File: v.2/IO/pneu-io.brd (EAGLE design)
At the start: 30.5 x 50.8 mm, 28 parts, among them IC3 ATMEGA328, Q1 16Mhz, U2 NCP1117-5

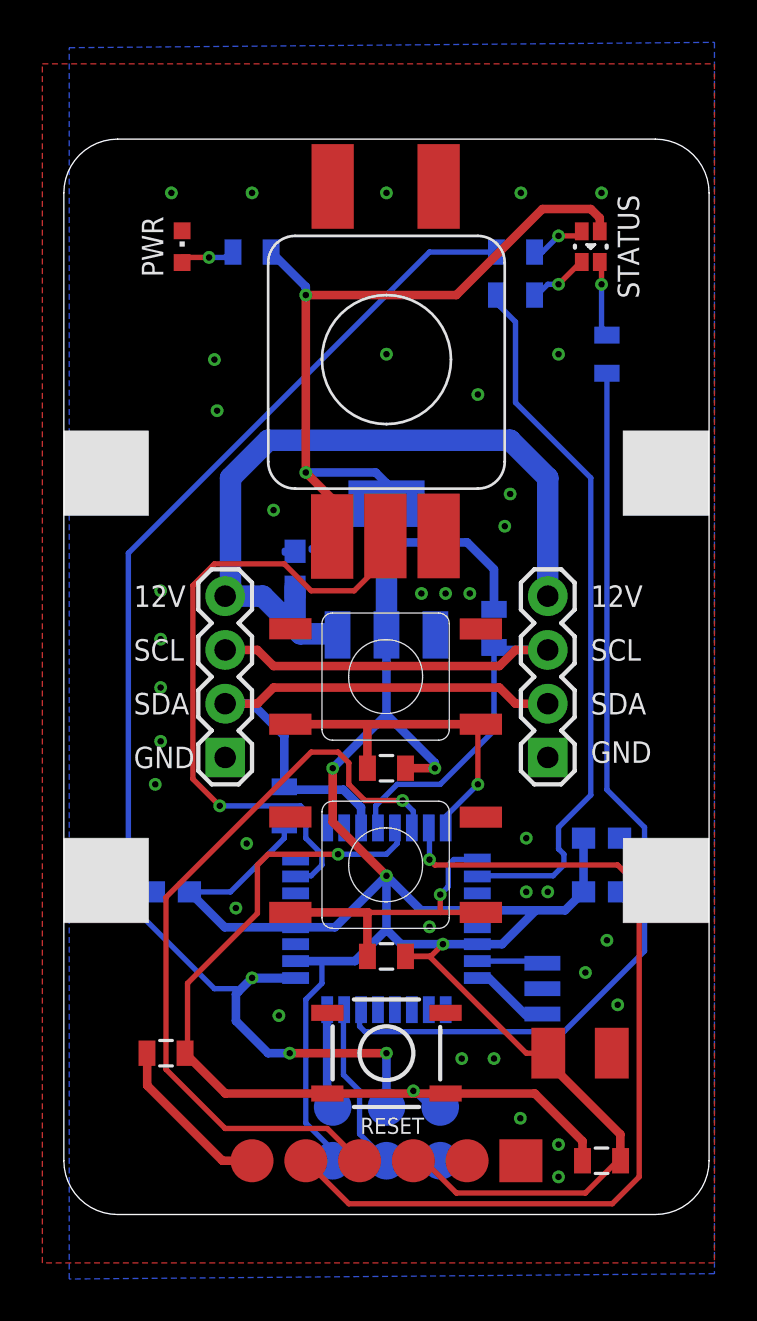
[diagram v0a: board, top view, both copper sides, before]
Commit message: minor changes
getting ready for production:

correct indicator led position on master board
add corner drills to slave boards
generate silk screens
adjust edge connector distance for better fit
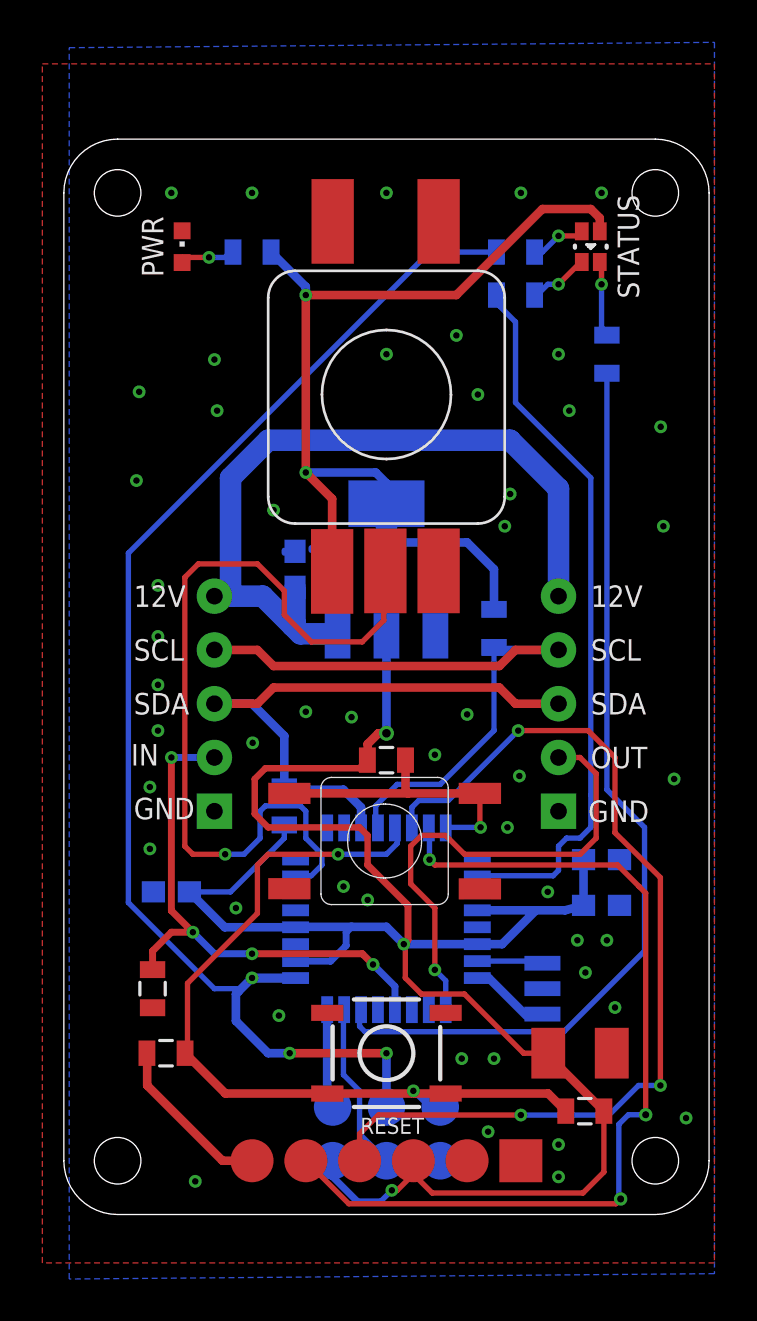
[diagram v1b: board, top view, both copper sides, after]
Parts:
- removed JP2, JP3: (no value), SparkFun-Connectors:1X04
- removed R2: 10K, SparkFun-Resistors:0805
- removed U$3: RS-014R05, digikey:SWITCH-11MM
- added R14: 10k, SparkFun-Resistors:0805
- added U$24, U$27: 1X05, digikey:1X05_TIGHT
- moved U$1 7.75 mm to (12.6, 17.7), turned to 0 degrees
- moved R3 2.47 mm to (22.1, 4.88)
- moved U$2 1.65 mm to (12.7, 39.0)
- moved C10 1.02 mm to (22.9, 16.8)
- moved C8 0.63 mm to (22.9, 14.6)
- moved R1 0.38 mm to (12.7, 21.5), turned to 0 degrees
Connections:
- removed net D5: IC3.9
- new net D5/OUT: IC3.9, U$27.P$4
- net +5V: no longer R2.1
- net D3/BTN: no longer R2.2, U$3.A, U$3.H
- net D8: now also R14.2, U$24.P$4
- net GND: now also R14.1, U$24.P$5, U$27.P$5; no longer JP2.1, JP3.1, U$3.B, U$3.D
- net SCL: now also U$24.P$3, U$27.P$3; no longer JP2.3, JP3.3
- net SDA: now also U$24.P$2, U$27.P$2; no longer JP2.2, JP3.2
- net VIN: now also U$24.P$1, U$27.P$1; no longer JP2.4, JP3.4
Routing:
- net D8: track 0.00 -> 25.6 mm, vias 0 -> 4
- net D5/OUT: track 0.00 -> 23.2 mm, vias 0 -> 1
- net D3/BTN: track 15.0 -> 0.00 mm, vias 1 -> 0
- net A0/POT: track 31.3 -> 42.2 mm
- net RX: track 36.2 -> 45.4 mm, vias 1 -> 3
- net +5V: track 152.0 -> 145.3 mm, vias 6 -> 5
- net D2/BTN: track 16.7 -> 13.9 mm
- net RESET: track 41.3 -> 39.0 mm
- net SDA: track 26.7 -> 28.2 mm
- net SCL: track 30.6 -> 32.1 mm
- net TX: track 42.8 -> 43.7 mm, vias 1 -> 3
- net VIN: track 35.8 -> 36.5 mm
- net GND: vias 36 -> 49
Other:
- board text added: "07/18/2016"
- board text added: "IN"
- board text added: "OUT"
- board text removed: "08/11/2015"

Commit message: small updates..
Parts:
- C5: device SparkFun-Capacitors:0805 -> SparkFun-Capacitors:0603-CAP
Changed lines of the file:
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@@
 <?xml version="1.0" encoding="utf-8"?>
 <!DOCTYPE eagle SYSTEM "eagle.dtd">
-<eagle version="7.4.0">
+<eagle version="7.6.0">
 <drawing>
 <settings>
@@
 </element>
 <element name="IC3" library="SparkFun" package="TQFP32-08" value="ATMEGA328" x="12.7" y="13.97" smashed="yes" rot="MR0"/>
-<element name="C5" library="SparkFun-Capacitors" package="0805" value="0.1uF" x="2.286" y="7.62" smashed="yes" rot="R180">
+<element name="C5" library="SparkFun-Capacitors" package="0603-CAP" value="0.1uF" x="2.286" y="7.62" smashed="yes" rot="R180">
 <attribute name="VALUE" x="1.016" y="5.842" size="0.762" layer="27"/>
 </element>
@@
 <wire x1="13.97" y1="5.715" x2="9.906" y2="5.715" width="0.4064" layer="1"/>
 <wire x1="9.906" y1="5.715" x2="5.091" y2="5.715" width="0.4064" layer="1"/>
-<wire x1="5.091" y1="5.715" x2="3.186" y2="7.62" width="0.4064" layer="1"/>
+<wire x1="5.091" y1="5.715" x2="3.136" y2="7.62" width="0.4064" layer="1"/>
 <wire x1="20.337071875" y1="5.715" x2="15.494" y2="5.715" width="0.4064" layer="1"/>
 <wire x1="13.208" y1="17.526" x2="13.208" y2="18.034" width="0.254" layer="16"/>
@@
 <wire x1="7.112" y1="17.018" x2="10.414" y2="17.018" width="0.254" layer="1"/>
 <wire x1="13.208" y1="18.034" x2="13.1" y2="18.2626" width="0.254" layer="16"/>
-<wire x1="3.302" y1="7.62" x2="3.186" y2="7.62" width="0.254" layer="1"/>
+<wire x1="3.302" y1="7.62" x2="3.136" y2="7.62" width="0.254" layer="1"/>
 <wire x1="14.732" y1="5.08" x2="15.24" y2="5.08" width="0.254" layer="16"/>
 <wire x1="13.97" y1="5.842" x2="14.732" y2="5.08" width="0.254" layer="16"/>
@@
 <wire x1="4.953" y1="2.54" x2="1.397" y2="6.096" width="0.4064" layer="1"/>
 <wire x1="1.397" y1="6.096" x2="1.397" y2="7.609" width="0.4064" layer="1"/>
-<wire x1="1.397" y1="7.609" x2="1.386" y2="7.62" width="0.4064" layer="1"/>
+<wire x1="1.397" y1="7.609" x2="1.436" y2="7.62" width="0.4064" layer="1"/>
 </signal>
 <signal name="RX">
